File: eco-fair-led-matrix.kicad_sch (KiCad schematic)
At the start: 41 parts, among them Q1 2N3904, Q2 2N3904, Q3 2N3904, Q4 2N3904, Q5 2N3904, U1 ATtiny84A-P

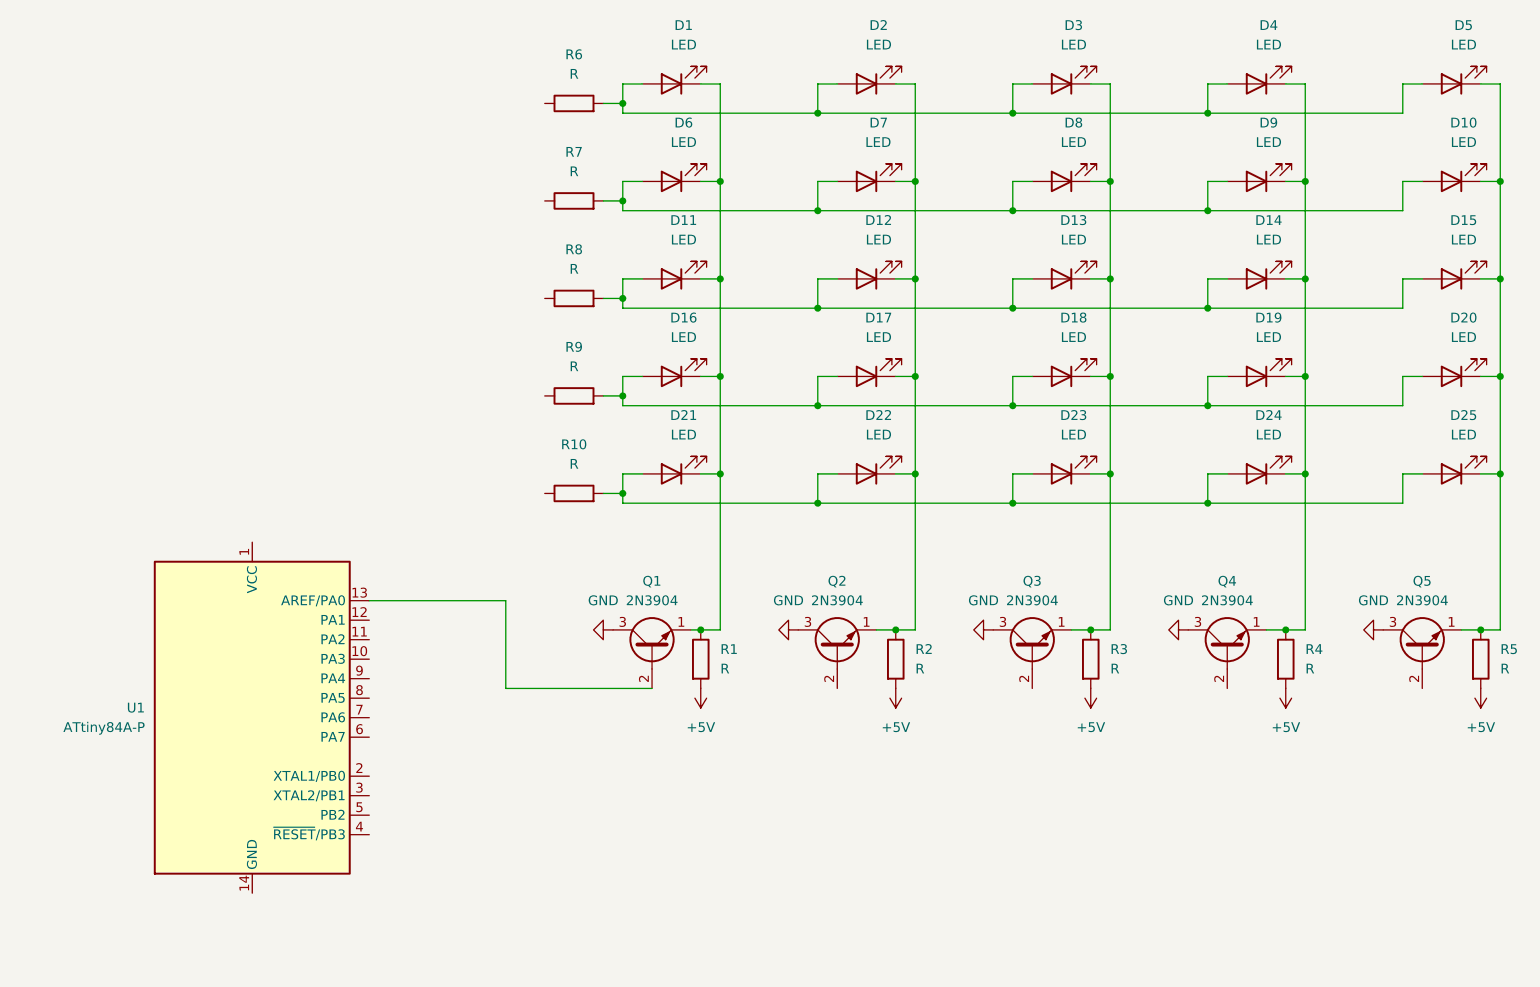
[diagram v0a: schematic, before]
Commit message: updated schematic with resistor values, started layout
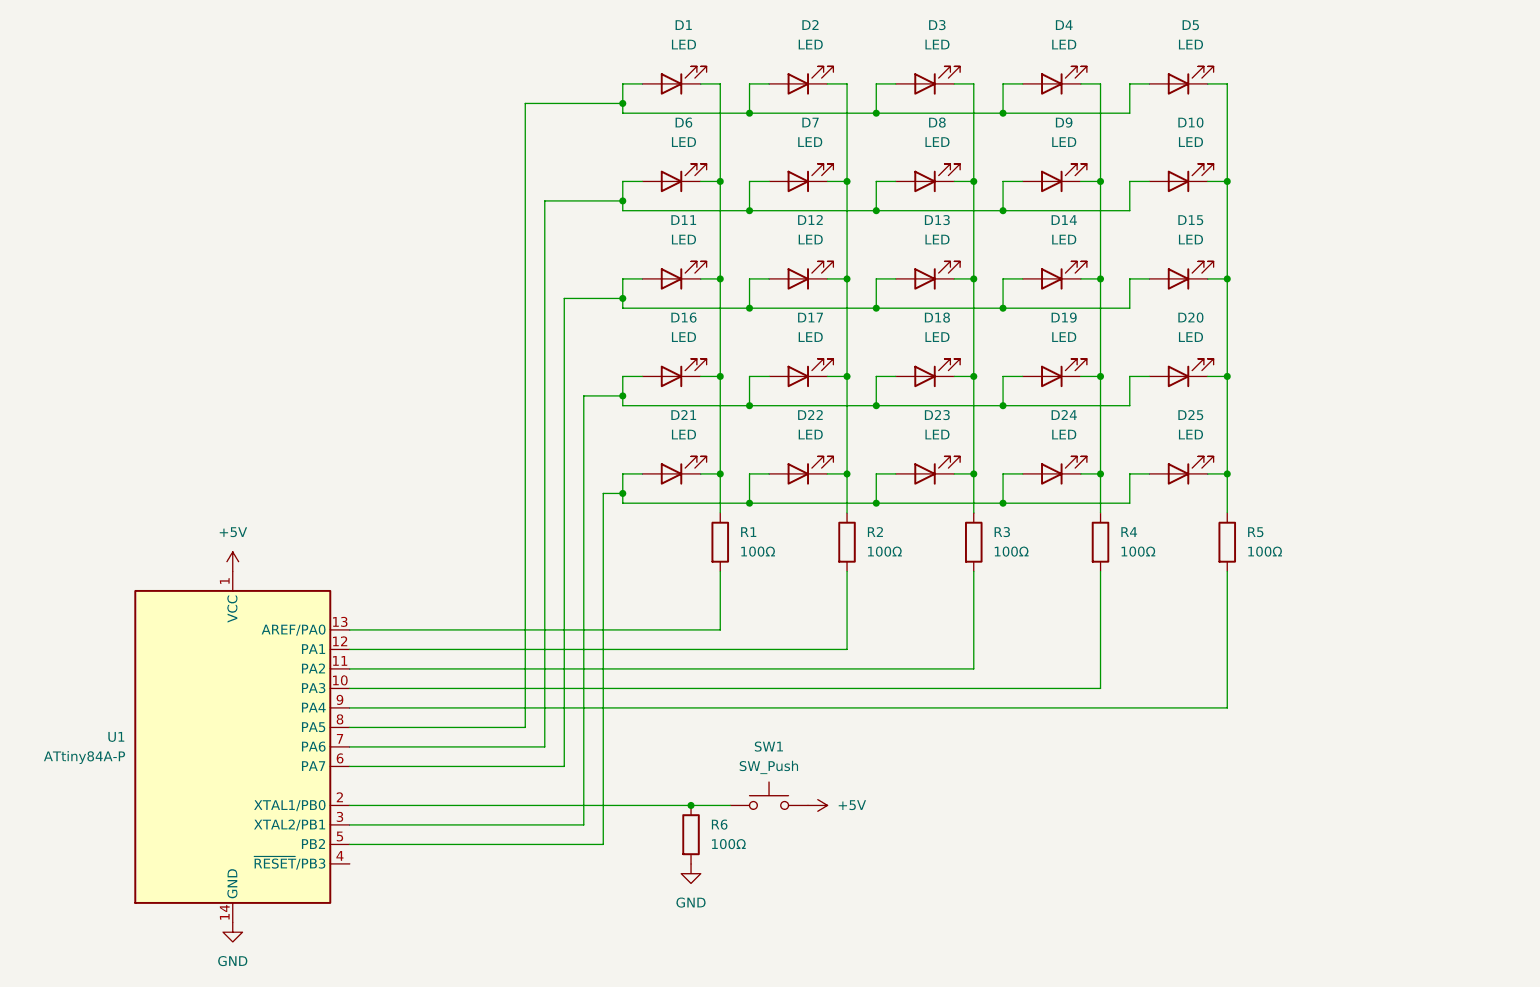
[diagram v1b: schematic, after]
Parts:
- removed Q1, Q2, Q3, Q4, Q5: 2N3904, Package_TO_SOT_THT:TO-92_Inline, symbol Transistor_BJT:2N3904
- removed R10, R7, R8, R9: R, symbol Device:R
- added SW1: SW_Push, symbol Switch:SW_Push
- R1, R2, R3, R4, R5, R6: value R -> 100Ω
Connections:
- net +5V: now also U1.1 (VCC), SW1.2; no longer R1.2, R2.2, R3.2, R4.2, R5.2
- net GND: now also R6.2, U1.14 (GND)
- net at D10.2 (A), D6.2 (A), D7.2 (A)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: now also U1.7 (PA6)
- net at U1.13 (AREF/PA0): now also R1.2
- net at D21.2 (A), D22.2 (A), D23.2 (A)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: now also U1.5 (PB2)
- net at D16.2 (A), D17.2 (A), D18.2 (A)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: now also U1.3 (XTAL2/PB1)
- net at D11.2 (A), D12.2 (A), D13.2 (A)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: now also U1.6 (PA7)
- net at U1.10 (PA3): now also R4.2
- net at U1.11 (PA2): now also R3.2
- net at U1.12 (PA1): now also R2.2
- net at U1.2 (XTAL1/PB0): now also R6.1, SW1.1
- net at U1.8 (PA5): now also D1.2 (A), D2.2 (A), D3.2 (A), D4.2 (A), D5.2 (A)
- net at U1.9 (PA4): now also R5.2
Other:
- title: (none) -> 5x5 LED Matrix
- moved on the sheet: D10, D12, D13, D14, D15, D17, D18, D19, D2, D20, D22, D23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
